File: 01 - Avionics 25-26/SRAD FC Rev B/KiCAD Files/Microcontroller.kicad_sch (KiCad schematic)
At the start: 6 parts, among them J1 Conn_ARM_SWD_TagConnect_TC2030

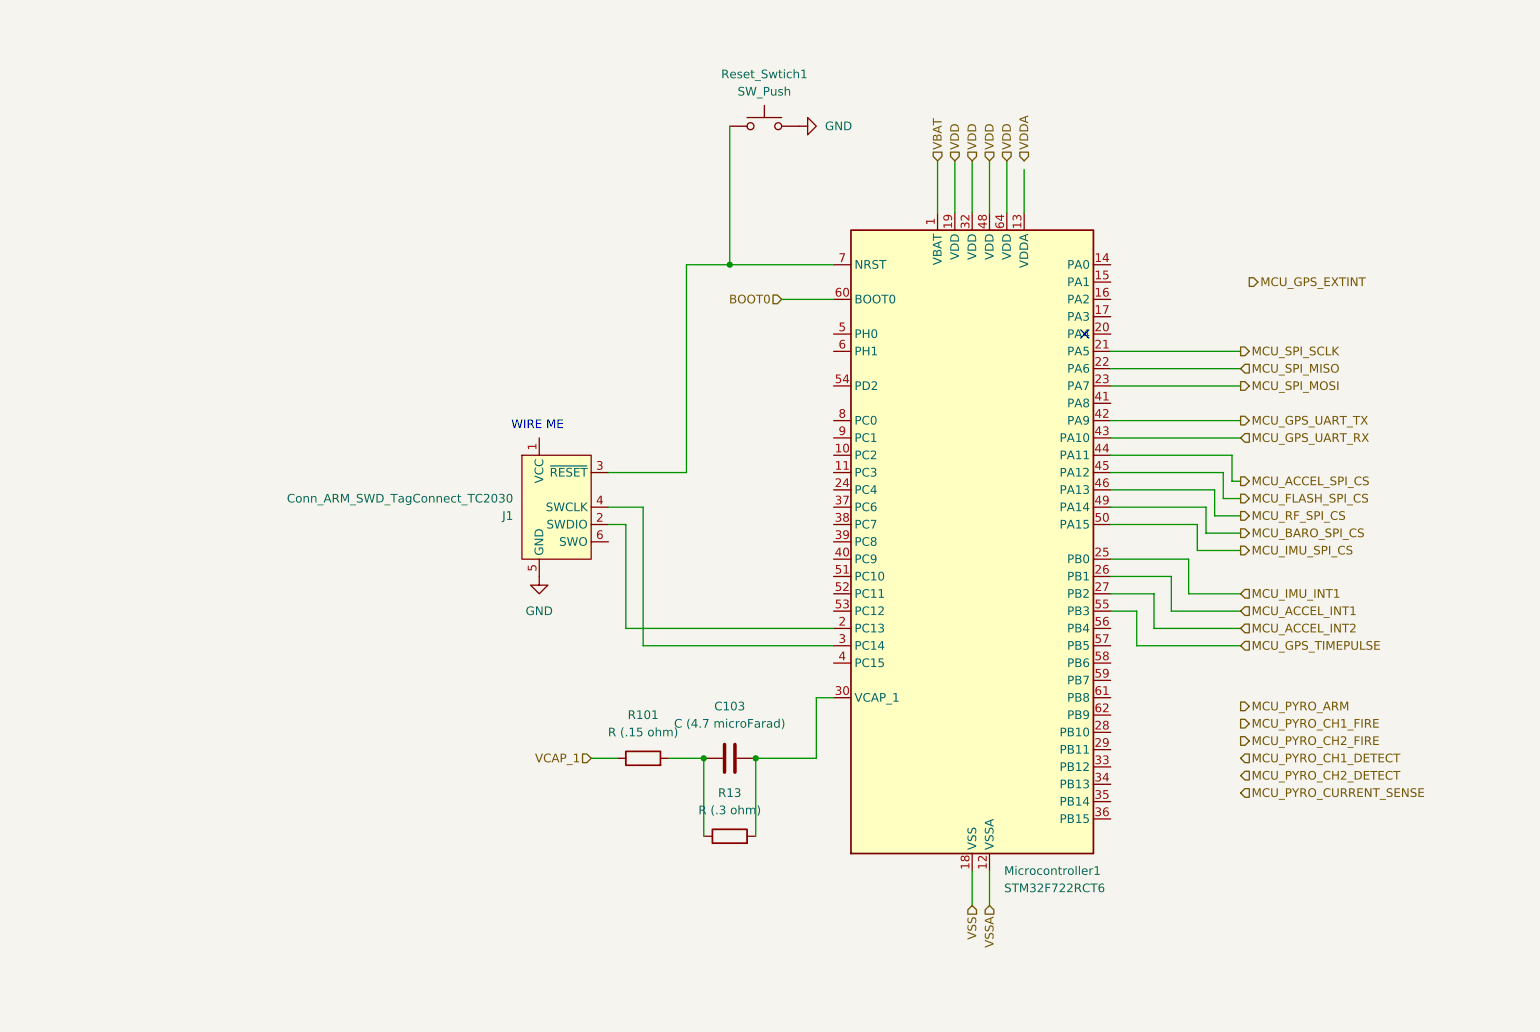
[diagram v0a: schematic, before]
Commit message: set up power conversion, wired power to mcu
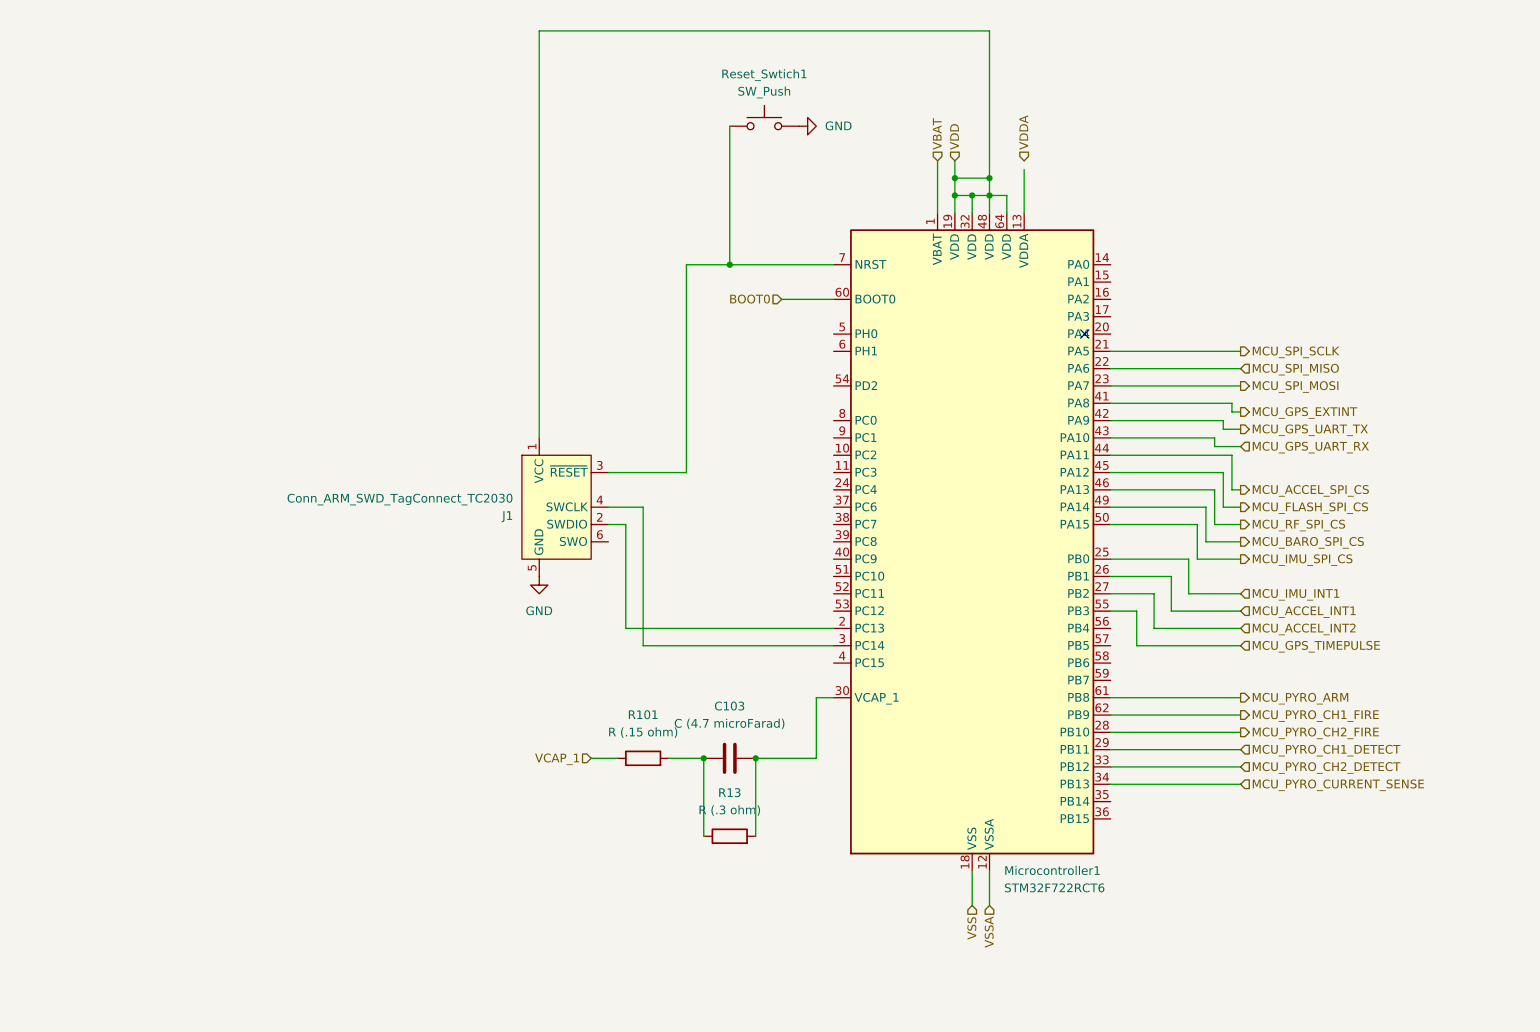
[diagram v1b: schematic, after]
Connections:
- net MCU_GPS_EXTINT: now also Microcontroller1.41 (PA8)
- net MCU_PYRO_ARM: now also Microcontroller1.61 (PB8)
- net MCU_PYRO_CH1_DETECT: now also Microcontroller1.29 (PB11)
- net MCU_PYRO_CH1_FIRE: now also Microcontroller1.62 (PB9)
- net MCU_PYRO_CH2_DETECT: now also Microcontroller1.33 (PB12)
- net MCU_PYRO_CH2_FIRE: now also Microcontroller1.28 (PB10)
- net MCU_PYRO_CURRENT_SENSE: now also Microcontroller1.34 (PB13)
- net VDD: now also J1.1 (VCC)
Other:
- note removed: "WIRE ME"

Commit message: fixes from notes from seth
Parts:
- added C17, C18, C19, C20: 1uF, Capacitor_SMD:C_0603_1608Metric_Pad1.08x0.95mm_HandSolder, symbol Device:C_Small
- added JP1: Jumper_2_Open, symbol Jumper:Jumper_2_Open
- C103: value C (4.7 microFarad) -> C (4700 nanoFarad)
- R101: value R (.15 ohm) -> R (150 milliOhm)
- R13: value R (.3 ohm) -> R (300 milliOhm)
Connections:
- net VSS is gone; now on net GND: Microcontroller1.18 (VSS), Microcontroller1.31 (VSS), Microcontroller1.47 (VSS), Microcontroller1.63 (VSS)
- net VSSA is gone; now on net GND: Microcontroller1.12 (VSSA)
- net GND: now also C17.1, C18.1, C19.1, C20.1
- net MCU_ACCEL_SPI_CS: now also Microcontroller1.14 (PA0); no longer Microcontroller1.44 (PA11)
- net MCU_BARO_SPI_CS: now also Microcontroller1.17 (PA3); no longer Microcontroller1.49 (PA14)
- net MCU_FLASH_SPI_CS: now also Microcontroller1.15 (PA1); no longer Microcontroller1.45 (PA12)
- net MCU_IMU_SPI_CS: now also Microcontroller1.20 (PA4); no longer Microcontroller1.50 (PA15)
- net MCU_RF_SPI_CS: now also Microcontroller1.16 (PA2); no longer Microcontroller1.46 (PA13)
- net VBAT: now also C19.2
- net VDD: now also C17.2, JP1.2 (B); no longer J1.1 (VCC)
- net VDDA: now also Microcontroller1.13 (VDDA), C18.2
- net at J1.3 (~{RESET}), Microcontroller1.7 (NRST), Reset_Swtich1.1: now also C20.2
- net at J1.2 (SWDIO): now also Microcontroller1.46 (PA13); no longer Microcontroller1.2 (PC13)
- net at J1.4 (SWCLK): now also Microcontroller1.49 (PA14); no longer Microcontroller1.3 (PC14)
- new net: J1.1 (VCC), JP1.1 (A)
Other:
- moved on the sheet: R101, Reset_Swtich1

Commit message: some fixes from seth's feedback
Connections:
- net MCU_PYRO_CURRENT_SENSE: no longer names the net of Microcontroller1.34 (PB13)
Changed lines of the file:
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@@
-	(wire
-		(pts
-			(xy 140.97 129.54) (xy 160.02 129.54)
-		)
-		(stroke
-			(width 0)
-			(type default)
-		)
-	)
 	(wire
 		(pts
@@
 			(width 0)
 			(type default)
-		)
-	)
-	(hierarchical_label "MCU_PYRO_CURRENT_SENSE"
-		(shape input)
-		(at 160.02 129.54 0)
-		(effects
-			(font
-				(size 1.27 1.27)
-			)
-			(justify left)
 		)
 	)
@@
 	)
 	(hierarchical_label "MCU_PYRO_ARM"
-		(shape output)
+		(shape input)
 		(at 160.02 116.84 0)
 		(effects

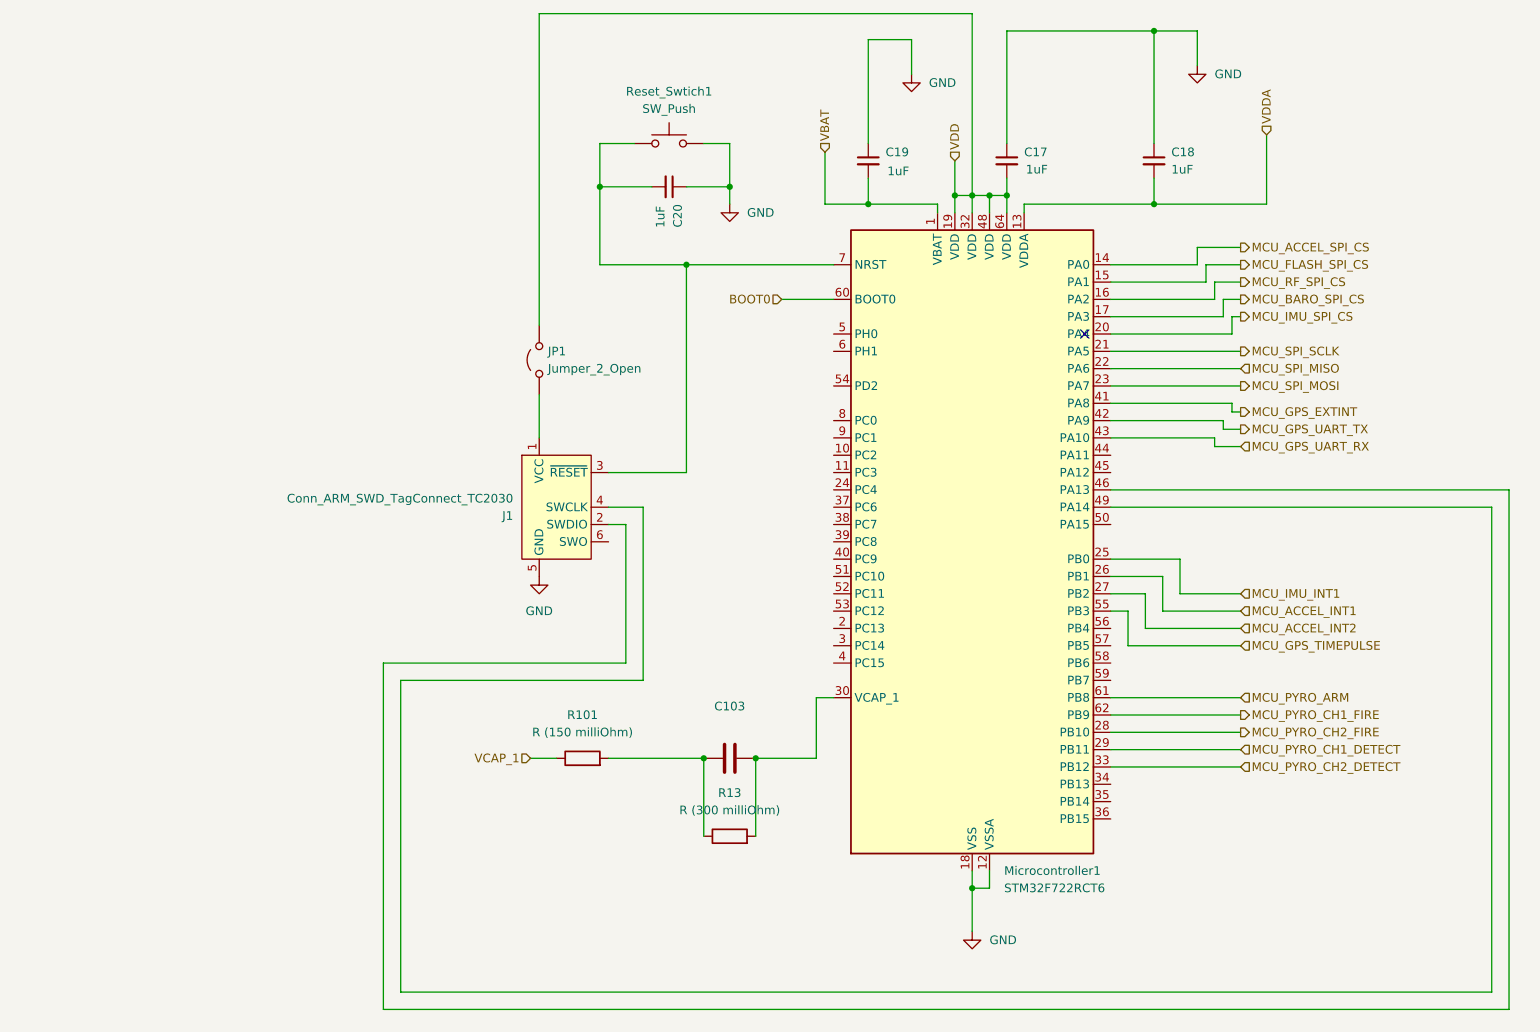
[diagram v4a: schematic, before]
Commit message: added uart port for data retrieval
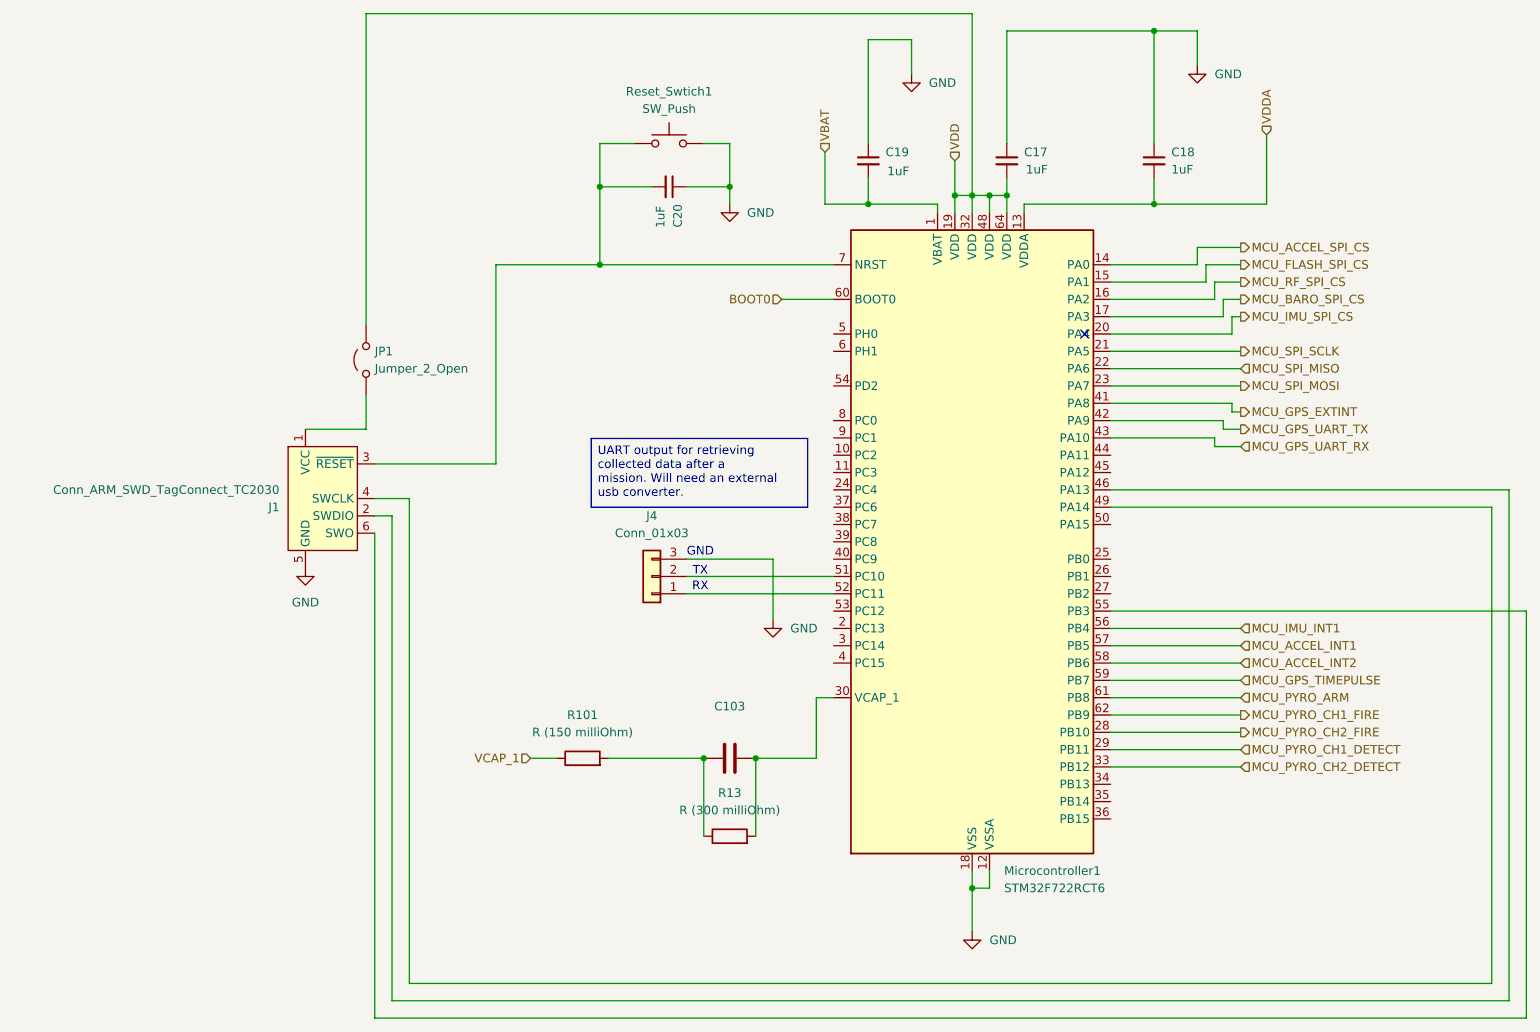
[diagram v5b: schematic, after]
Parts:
- added J4: Conn_01x03, symbol Connector_Generic:Conn_01x03
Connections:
- net GND: now also J4.3 (Pin_3)
- net MCU_ACCEL_INT1: now also Microcontroller1.57 (PB5); no longer Microcontroller1.26 (PB1)
- net MCU_ACCEL_INT2: now also Microcontroller1.58 (PB6); no longer Microcontroller1.27 (PB2)
- net MCU_GPS_TIMEPULSE: now also Microcontroller1.59 (PB7); no longer Microcontroller1.55 (PB3)
- net MCU_IMU_INT1: now also Microcontroller1.56 (PB4); no longer Microcontroller1.25 (PB0)
- net at J1.6 (SWO): now also Microcontroller1.55 (PB3)
- net at Microcontroller1.51 (PC10): now also J4.2 (Pin_2)
- net at Microcontroller1.52 (PC11): now also J4.1 (Pin_1)
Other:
- note added: "GND"
- note added: "RX"
- note added: "TX"
- moved on the sheet: J1, JP1
